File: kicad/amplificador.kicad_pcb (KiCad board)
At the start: 2 copper layers, 55 parts, among them Q1 BC557, Q10 BC547, Q11 BC547, Q12 BC557, Q13 BC547, Q14 BC557, Q15 TIP41C, Q16 TIP41C, Q17 TIP42C, Q18 TIP42C, Q2 BC547, Q3 BC557, Q4 BC547, Q5 BC557, Q6 BC557, Q7 BC547, Q8 BC557, Q9 BC547

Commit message: pcb Kicad actualizado
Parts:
- moved D4 360.7 mm to (203.2, 123.8)
- moved D3 327.1 mm to (205.7, 64.8)
- moved D6 264.2 mm to (266.7, 84.5)
- moved Q13 259.2 mm to (226.1, 81.3), turned to 270 degrees
- moved R15 255.5 mm to (112.4, 122.6), turned to 270 degrees
- moved Q17 228.8 mm to (246.4, 108.6), turned to 90 degrees
- moved Q10 214.9 mm to (179.1, 103.5), turned to 180 degrees
- moved Q16 203.0 mm to (245.7, 83.8), turned to 270 degrees
- moved R16 184.1 mm to (188.6, 113.7)
- moved R17 182.7 mm to (199.6, 117.5)
- moved Q12 175.9 mm to (226.7, 125.1), turned to 90 degrees
- moved Q18 171.9 mm to (244.5, 122.6), turned to 270 degrees
- moved R20 158.0 mm to (214.2, 111.8), turned to 180 degrees
- moved R8 157.2 mm to (214.2, 100.3), turned to 0 degrees
- moved R11 155.4 mm to (214.4, 104.8), turned to 0 degrees
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
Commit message: Primer ruteo
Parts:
- moved D5 91.3 mm to (184.2, 113.0)
- moved D6 90.4 mm to (176.8, 94.0)
- moved R21 85.4 mm to (176.3, 79.3)
- moved R22 81.4 mm to (176.5, 128.8)
- moved Q15 79.0 mm to (167.9, 77.1)
- moved Q16 78.2 mm to (167.9, 91.3)
- moved R23 78.2 mm to (168.5, 104.0)
- moved Q18 78.0 mm to (166.6, 127.5)
- moved Q17 77.3 mm to (169.7, 118.1)
- moved Q6 75.9 mm to (133.2, 79.5)
- moved D4 71.8 mm to (131.6, 129.4)
- moved Q12 71.6 mm to (155.2, 129.4), turned to 0 degrees
- moved Q11 71.1 mm to (156.8, 82.2)
- moved Q13 69.9 mm to (156.8, 91.3)
- moved Q14 69.9 mm to (157.5, 123.1)
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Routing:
- net V-: track 0.00 -> 149.8 mm
- net V+: track 0.00 -> 86.2 mm
- net Net-(C5-Pad2): track 0.00 -> 71.6 mm
- net Net-(Q5-Pad2): track 0.00 -> 62.1 mm, vias 0 -> 1
- net GND: track 0.00 -> 57.6 mm
- net Net-(C6-Pad2): track 0.00 -> 57.2 mm
- net Net-(C6-Pad1): track 0.00 -> 46.9 mm
- net Net-(D5-Pad2): track 0.00 -> 36.1 mm
- net Net-(Q14-Pad3): track 0.00 -> 33.9 mm
- net Net-(C2-Pad1): track 0.00 -> 33.3 mm
- net Net-(D6-Pad1): track 0.00 -> 31.1 mm
- net Net-(C5-Pad1): track 0.00 -> 29.9 mm
- net Net-(Q13-Pad3): track 0.00 -> 29.2 mm
- net Net-(Q7-Pad3): track 0.00 -> 25.2 mm
- net Net-(D3-Pad1): track 0.00 -> 23.8 mm
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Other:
- board outline added: 175.9 x 76.8 mm

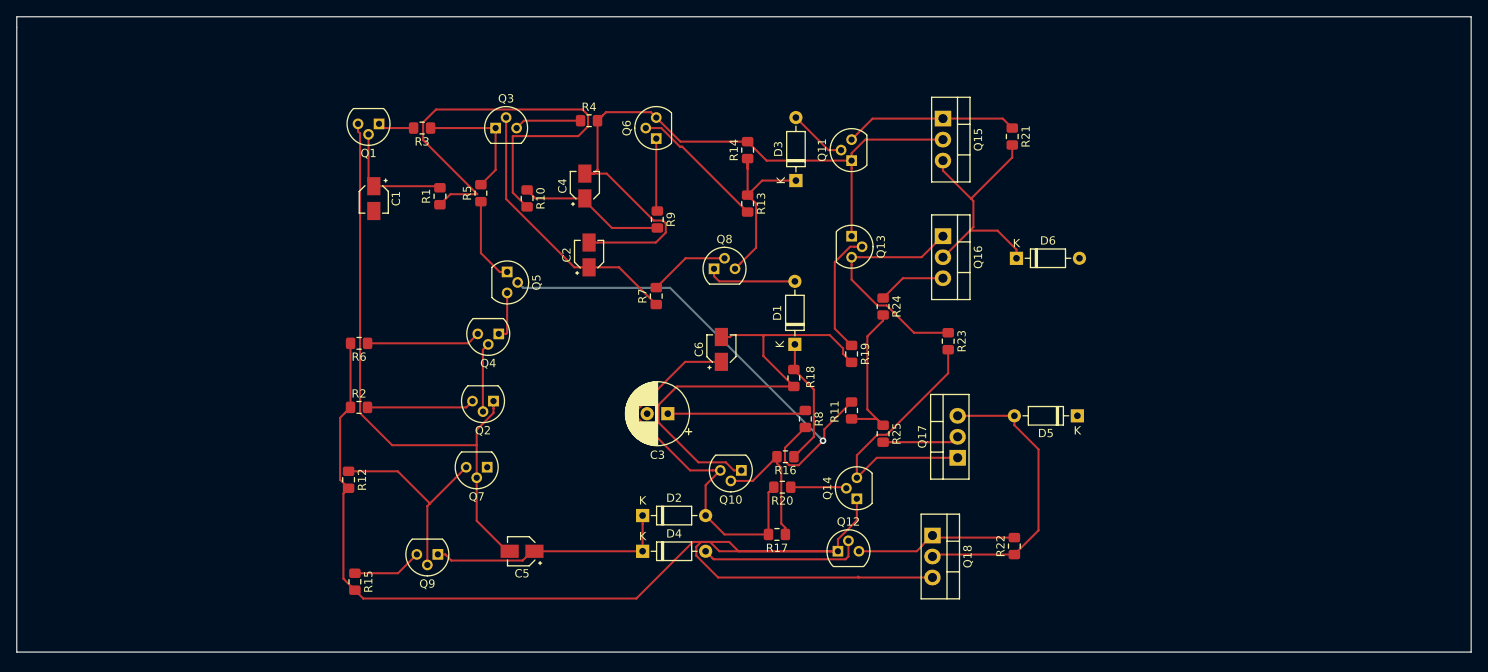
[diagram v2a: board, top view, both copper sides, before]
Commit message: Actualización del pcb
Se acercaró el multiplicador de vbe a los transistores de potencia por acoplamiento térmico. Se dejó lugar para montarlos sobre un disipador.
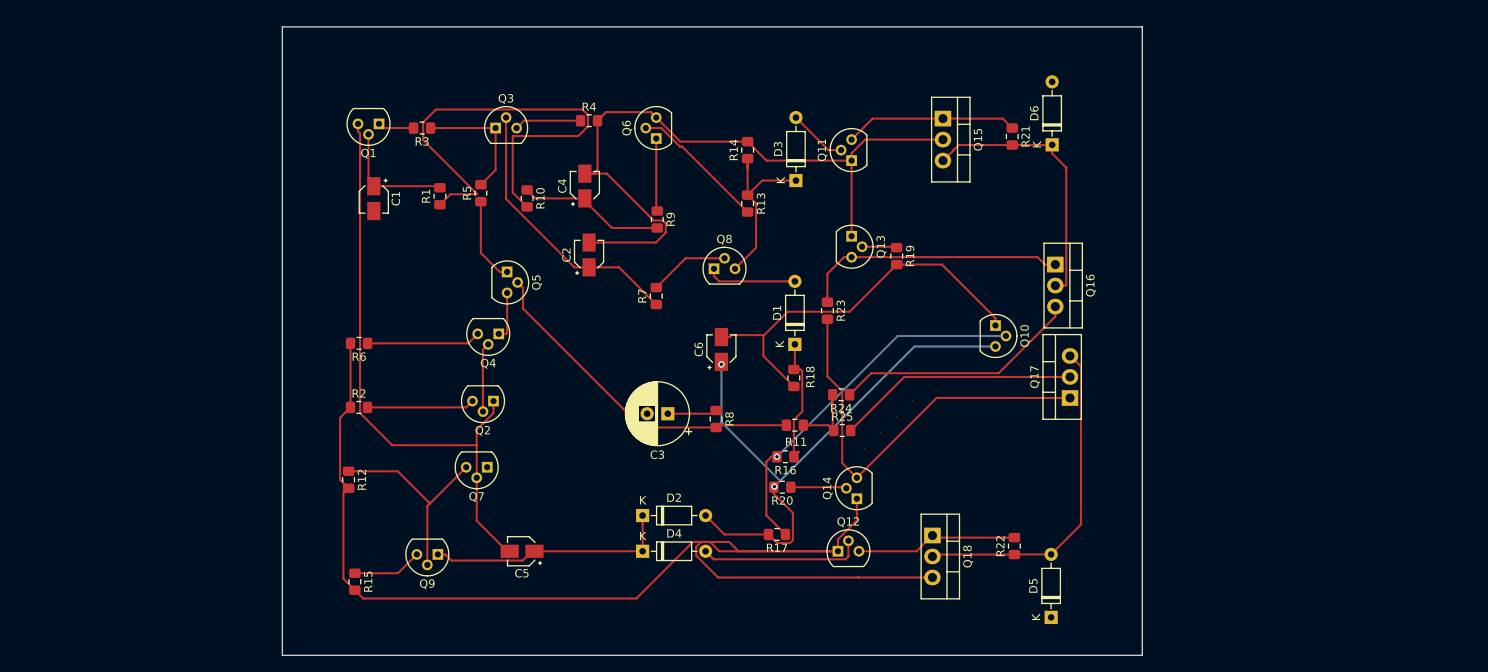
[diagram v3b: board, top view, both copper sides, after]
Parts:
- moved Q10 35.4 mm to (174.2, 102.1), turned to 270 degrees
- moved D5 24.6 mm to (181.0, 137.4), turned to 90 degrees
- moved Q17 15.4 mm to (183.3, 110.9)
- moved R23 15.1 mm to (153.9, 100.3)
- moved D6 14.4 mm to (181.1, 80.3), turned to 90 degrees
- moved Q16 14.0 mm to (181.5, 94.7)
- moved R19 13.0 mm to (162.3, 93.7)
- moved R24 11.8 mm to (155.6, 110.5), turned to 180 degrees
- moved R8 10.8 mm to (140.5, 113.4)
- moved R11 7.09 mm to (150.0, 114.2), turned to 180 degrees
- moved R25 4.96 mm to (155.7, 114.8), turned to 0 degrees
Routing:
- net Net-(Q10-Pad2): track 17.3 -> 45.7 mm, vias 0 -> 1
- net Net-(C6-Pad1): track 46.9 -> 71.1 mm, vias 0 -> 3
- net Net-(Q16-Pad3): track 8.23 -> 30.0 mm
- net Net-(Q5-Pad2): track 62.1 -> 41.7 mm, vias 1 -> 0
- net Net-(Q17-Pad2): track 9.29 -> 29.2 mm
- net Net-(Q14-Pad3): track 33.9 -> 50.4 mm
- net Net-(C3-Pad1): track 16.8 -> 6.00 mm
- net Net-(Q13-Pad2): track 15.0 -> 4.24 mm
- net Vout: track 19.0 -> 8.31 mm
- net Net-(C6-Pad2): track 57.2 -> 48.0 mm
- net Net-(D5-Pad2): track 36.1 -> 40.5 mm
- net Net-(Q13-Pad3): track 29.2 -> 32.2 mm
- net Net-(D6-Pad1): track 31.1 -> 33.0 mm
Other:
- board size 175.9 x 76.8 mm -> 104 x 76 mm

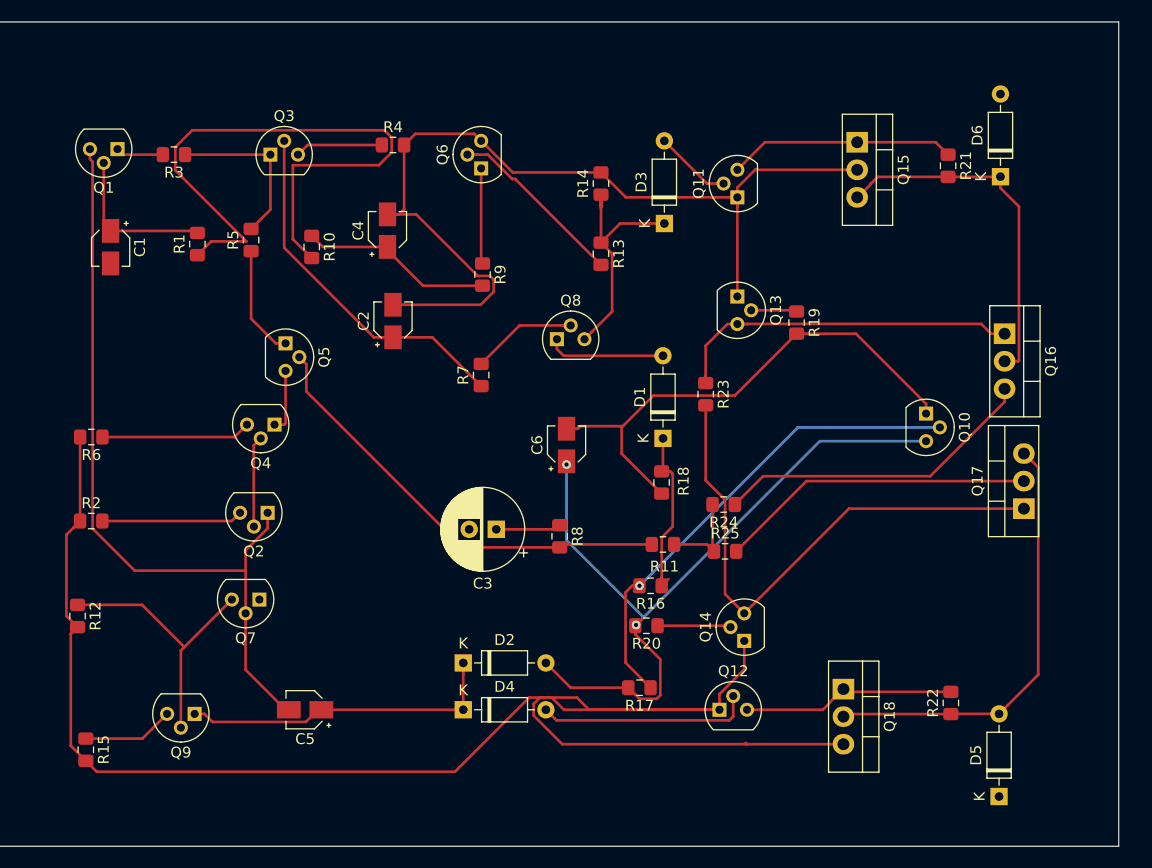
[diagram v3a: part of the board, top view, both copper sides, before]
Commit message: Ruteo del esquemático modificado
Capacitor a -30V, encapsulados finales, capacitor de entrada de poliéster.
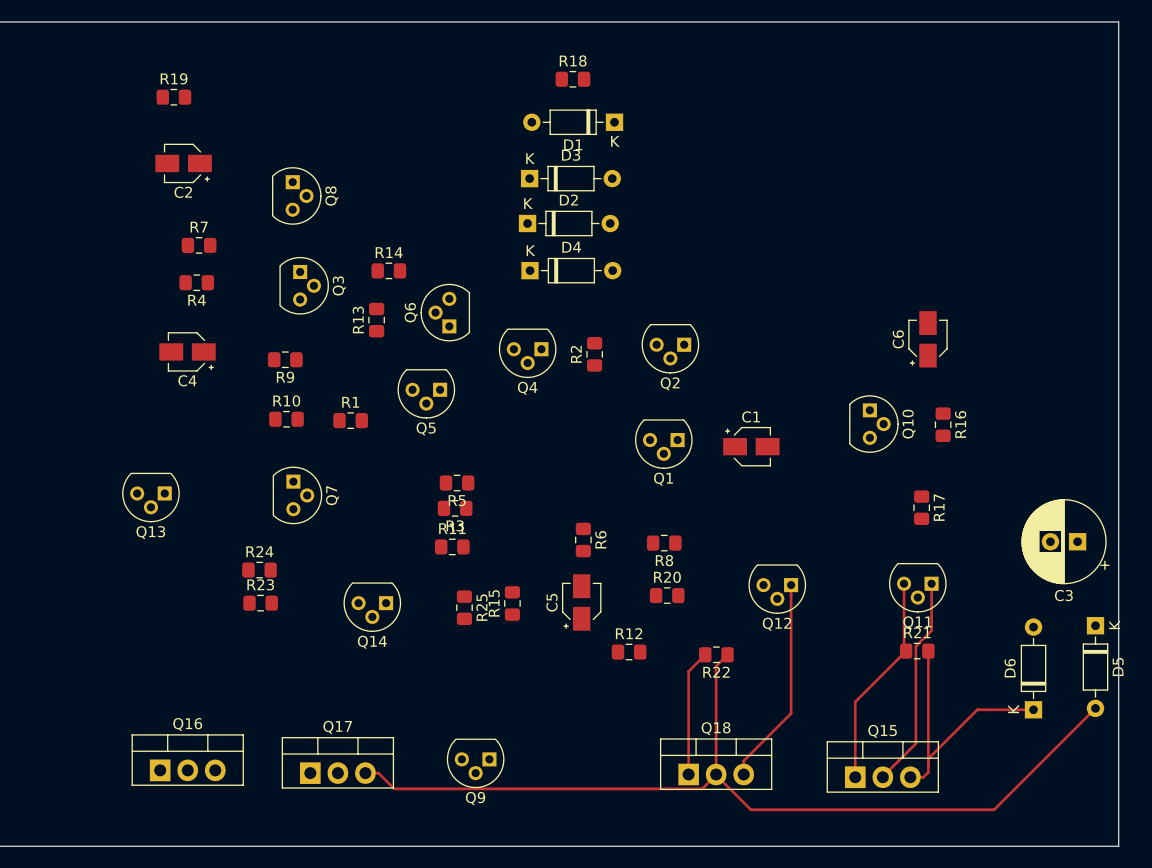
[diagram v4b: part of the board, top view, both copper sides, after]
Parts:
- moved Q16 87.6 mm to (103.6, 135.0), turned to 0 degrees
- moved Q17 70.2 mm to (117.5, 135.3), turned to 0 degrees
- moved C1 61.9 mm to (158.1, 105.2), turned to 0 degrees
- moved R19 61.1 mm to (104.9, 72.9), turned to 0 degrees
- moved Q15 58.5 mm to (167.7, 135.6), turned to 0 degrees
- moved Q1 58.2 mm to (151.3, 104.5)
- moved Q13 55.8 mm to (104.1, 109.5), turned to 180 degrees
- moved C3 53.6 mm to (188.2, 113.9)
- moved R12 51.0 mm to (146.9, 124.1), turned to 0 degrees
- moved D6 49.2 mm to (184.2, 129.4)
- moved R2 48.9 mm to (143.7, 96.6), turned to 90 degrees
- moved R6 46.3 mm to (142.6, 113.8), turned to 270 degrees
- moved R23 45.3 mm to (112.9, 119.6), turned to 0 degrees
- moved R21 44.8 mm to (173.4, 124.0), turned to 0 degrees
- moved R24 43.2 mm to (112.8, 116.5), turned to 0 degrees
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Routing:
- net V-: track 149.8 -> 19.3 mm
- net Net-(C5-Pad2): track 71.6 -> 0.00 mm
- net Net-(C6-Pad1): track 71.1 -> 0.00 mm, vias 3 -> 0
- net V+: track 86.2 -> 19.7 mm
- net GND: track 57.6 -> 0.00 mm
- net Net-(Q14-Pad3): track 50.4 -> 0.00 mm
- net Net-(C6-Pad2): track 48.0 -> 0.00 mm
- net Net-(Q10-Pad2): track 45.7 -> 0.00 mm, vias 1 -> 0
- net Net-(D5-Pad2): track 40.5 -> 85.2 mm
- net Net-(Q5-Pad2): track 41.7 -> 0.00 mm
- net Net-(C2-Pad1): track 33.3 -> 0.00 mm
- net Net-(Q13-Pad3): track 32.2 -> 0.00 mm
- net Net-(Q16-Pad3): track 30.0 -> 0.00 mm
- net Net-(C5-Pad1): track 29.9 -> 0.00 mm
- net Net-(Q17-Pad2): track 29.2 -> 0.00 mm
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
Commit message: viaje en el tiempo... el commit anterior esta roto
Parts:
- moved Q16 87.6 mm to (181.5, 94.7), turned to 270 degrees
- moved Q17 70.2 mm to (183.3, 110.9), turned to 90 degrees
- moved C1 61.9 mm to (99.1, 86.8), turned to 270 degrees
- moved R19 61.1 mm to (162.3, 93.7), turned to 270 degrees
- moved Q15 58.5 mm to (167.9, 77.1), turned to 270 degrees
- moved Q1 58.2 mm to (99.7, 77.7)
- moved Q13 55.8 mm to (156.8, 91.3), turned to 270 degrees
- moved C3 53.6 mm to (134.6, 112.8)
- moved R12 51.0 mm to (96.0, 120.8), turned to 270 degrees
- moved D6 49.2 mm to (181.1, 80.3)
- moved R2 48.9 mm to (97.3, 112.0), turned to 0 degrees
- moved R6 46.3 mm to (97.3, 104.3), turned to 180 degrees
- moved R23 45.3 mm to (153.9, 100.3), turned to 270 degrees
- moved R21 44.8 mm to (176.3, 79.3), turned to 270 degrees
- moved R24 43.2 mm to (155.6, 110.5), turned to 180 degrees
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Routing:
- net V-: track 19.3 -> 149.8 mm
- net Net-(C5-Pad2): track 0.00 -> 71.6 mm
- net Net-(C6-Pad1): track 0.00 -> 71.1 mm, vias 0 -> 3
- net V+: track 19.7 -> 86.2 mm
- net GND: track 0.00 -> 57.6 mm
- net Net-(Q14-Pad3): track 0.00 -> 50.4 mm
- net Net-(C6-Pad2): track 0.00 -> 48.0 mm
- net Net-(Q10-Pad2): track 0.00 -> 45.7 mm, vias 0 -> 1
- net Net-(D5-Pad2): track 85.2 -> 40.5 mm
- net Net-(Q5-Pad2): track 0.00 -> 41.7 mm
- net Net-(C2-Pad1): track 0.00 -> 33.3 mm
- net Net-(Q13-Pad3): track 0.00 -> 32.2 mm
- net Net-(Q16-Pad3): track 0.00 -> 30.0 mm
- net Net-(C5-Pad1): track 0.00 -> 29.9 mm
- net Net-(Q17-Pad2): track 0.00 -> 29.2 mm
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
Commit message: Final de clase viernes  28 de junio
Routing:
- net GND: track 57.6 -> 0.00 mm
- net Net-(C6-Pad1): track 71.1 -> 75.5 mm, vias 3 -> 2
- added copper zone on B.Cu, net GND

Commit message: carpeta kicad con esquematico con todos los encapsulados correctos, jumpers, pines de alimentacion y medicon. pcb a medio hacer
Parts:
- removed D1, D2: 1N4148, Diode_THT:D_DO-35_SOD27_P7.62mm_Horizontal
- added J1: Screw_Terminal_01x01, Connector_Wire:SolderWirePad_1x01_Drill0.8mm, F.Cu at (10.2, 101.6)
- added J10: Conn_01x01_Male, Connector_Pin:Pin_D0.7mm_L6.5mm_W1.8mm_FlatFork, F.Cu at (201.9, -12.7)
- added J11: Conn_01x01_Male, Connector_Pin:Pin_D0.7mm_L6.5mm_W1.8mm_FlatFork, F.Cu at (203.7, 116.3)
- added J12: Conn_01x01_Male, Connector_Pin:Pin_D0.7mm_L6.5mm_W1.8mm_FlatFork, F.Cu at (196.3, 128.0)
- added J13: Conn_01x01_Male, Connector_Pin:Pin_D0.7mm_L6.5mm_W1.8mm_FlatFork, F.Cu at (232.4, 71.1)
- added J14: Conn_01x01_Male, Connector_Pin:Pin_D0.7mm_L6.5mm_W1.8mm_FlatFork, F.Cu at (203.7, 122.9)
- added J15: Conn_01x01_Male, Connector_Pin:Pin_D0.7mm_L6.5mm_W1.8mm_FlatFork, F.Cu at (225.3, 104.6)
- added J16: Screw_Terminal_01x01, Connector_Wire:SolderWirePad_1x01_Drill0.8mm, F.Cu at (193.3, 135.4)
- added J17: Screw_Terminal_01x01, Connector_Wire:SolderWirePad_1x01_Drill0.8mm, F.Cu at (232.1, 98.0)
- added J2: Conn_01x01_Male, Connector_Pin:Pin_D0.7mm_L6.5mm_W1.8mm_FlatFork, F.Cu at (35.6, 83.8)
- added J3: Conn_01x01_Male, Connector_Pin:Pin_D0.7mm_L6.5mm_W1.8mm_FlatFork, F.Cu at (35.6, 134.6)
- added J4: Conn_01x01_Male, Connector_Pin:Pin_D0.7mm_L6.5mm_W1.8mm_FlatFork, F.Cu at (43.2, 33.0)
- added J5: Conn_01x01_Male, Connector_Pin:Pin_D0.7mm_L6.5mm_W1.8mm_FlatFork, F.Cu at (59.7, 83.8)
- added J6: Conn_01x01_Male, Connector_Pin:Pin_D0.7mm_L6.5mm_W1.8mm_FlatFork, F.Cu at (209.7, 109.8)
- added J7: Screw_Terminal_01x01, Connector_Wire:SolderWirePad_1x01_Drill0.8mm, F.Cu at (223.5, 1.27)
- added J8: Screw_Terminal_01x01, Connector_Wire:SolderWirePad_1x01_Drill0.8mm, F.Cu at (189.7, 128.9)
- added J9: Conn_01x01_Male, Connector_Pin:Pin_D0.7mm_L6.5mm_W1.8mm_FlatFork, F.Cu at (134.6, 34.3)
- added JP1: Jumper_NO_Small, kicad:SolderJumper-2_P1.3mm_Open_Pad1.0x1.5mm, F.Cu at (115.6, 99.1)
- added JP2: Jumper_NO_Small, kicad:SolderJumper-2_P1.3mm_Open_Pad1.0x1.5mm, F.Cu at (331.5, 86.4)
- added JP3: Jumper_NO_Small, kicad:SolderJumper-2_P1.3mm_Open_Pad1.0x1.5mm, F.Cu at (151.1, 106.7)
- added JP4: Jumper_NO_Small, kicad:SolderJumper-2_P1.3mm_Open_Pad1.0x1.5mm, F.Cu at (235.6, 142.2)
- added JP5: Jumper_NO_Small, kicad:SolderJumper-2_P1.3mm_Open_Pad1.0x1.5mm, F.Cu at (211.5, 14.0)
- added U1: LM385D-1.2, Package_SO:SOIC-8_3.9x4.9mm_P1.27mm, F.Cu at (273.0, 95.9)
- added U2: LM385D-1.2, Package_SO:SOIC-8_3.9x4.9mm_P1.27mm, F.Cu at (176.5, 3.81)
- C1: value 47u -> 10u; footprint Capacitor_SMD:CP_Elec_3x5.3 -> Capacitor_THT:C_Disc_D10.0mm_W2.5mm_P5.00mm
- D5, D6: value 1N4148 -> 1N5822; footprint Diode_THT:D_DO-35_SOD27_P7.62mm_Horizontal -> Diode_THT:D_DO-201AD_P15.24mm_Horizontal
- Q1, Q3, Q5, Q6, Q8: value BC557 -> MPSA92; footprint Package_TO_SOT_THT:TO-92 -> Package_TO_SOT_THT:TO-92_Inline
- Q10, Q2, Q4, Q7, Q9: value BC547 -> MPSA42; footprint Package_TO_SOT_THT:TO-92 -> Package_TO_SOT_THT:TO-92_Inline
- Q11, Q13: value BC547 -> BD135; footprint Package_TO_SOT_THT:TO-92 -> Package_TO_SOT_THT:TO-126-3_Vertical
- Q12, Q14: value BC557 -> BD136; footprint Package_TO_SOT_THT:TO-92 -> Package_TO_SOT_THT:TO-126-3_Vertical
- Q15, Q16: value TIP41C -> 2SD1047; footprint Package_TO_SOT_THT:TO-220-3_Vertical -> Package_TO_SOT_THT:TO-3PB-3_Vertical
- Q17, Q18: value TIP42C -> 2SB817; footprint Package_TO_SOT_THT:TO-220-3_Vertical -> Package_TO_SOT_THT:TO-3PB-3_Vertical
- R11: value 400 -> 12k
- R2, R6: value 1 -> 68
- R8: value 9.6k -> 470
- moved D4 218.7 mm to (185.4, -82.5)
- moved Q14 207.6 mm to (353.1, 53.3), turned to 0 degrees
- moved R25 203.6 mm to (359.2, 106.7)
- moved D3 201.8 mm to (351.8, 92.7), turned to 0 degrees
- moved R15 201.6 mm to (298.2, 142.2), turned to 0 degrees
- moved Q11 190.3 mm to (344.2, 115.6), turned to 0 degrees
- moved D5 190.2 mm to (336.6, 27.9), turned to 0 degrees
- moved C4 188.5 mm to (210.6, -82.5), turned to 0 degrees
- moved Q12 187.0 mm to (142.2, -57.1)
- moved R12 170.3 mm to (265.7, 135.9), turned to 0 degrees
- moved D6 166.9 mm to (348.0, 83.8), turned to 0 degrees
- moved Q17 165.9 mm to (332.4, 38.1), turned to 0 degrees
- moved R13 161.0 mm to (292.1, 151.1), turned to 0 degrees
- moved Q6 156.1 mm to (275.6, 143.5), turned to 0 degrees
- moved C6 153.3 mm to (146.1, -48.3), turned to 0 degrees
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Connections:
- C1 pad 2: Vin -> Net-(C1-Pad2)
- C2 pad 2: V+ -> Net-(C2-Pad2)
- C4 pad 2: V+ -> Net-(C2-Pad2)
- D5 pad 1: V1- -> Net-(D5-Pad1)
- D6 pad 2: V1+ -> Net-(D6-Pad2)
- Q10 pad 1: Net-(C6-Pad2) -> Net-(Q10-Pad1)
- Q10 pad 3: Net-(C6-Pad1) -> Net-(C5-Pad1)
- Q11 pad 1: V+ -> Net-(Q11-Pad1)
- Q11 pad 2: Net-(D3-Pad2) -> Net-(C2-Pad2)
- Q11 pad 3: Net-(Q11-Pad3) -> Net-(D3-Pad2)
- Q12 pad 1: V- -> Net-(Q12-Pad1)
- Q12 pad 2: Net-(D4-Pad2) -> Net-(J7-Pad1)
- Q12 pad 3: Net-(Q12-Pad3) -> Net-(D4-Pad2)
- Q13 pad 1: V+ -> Net-(J12-Pad1)
- Q13 pad 2: Net-(Q13-Pad2) -> Net-(C2-Pad2)
- Q13 pad 3: Net-(Q13-Pad3) -> Net-(J10-Pad1)
- Q14 pad 1: V- -> Net-(J13-Pad1)
- Q14 pad 2: Net-(Q14-Pad2) -> Net-(J7-Pad1)
- Q14 pad 3: Net-(Q14-Pad3) -> Net-(J11-Pad1)
- Q15 pad 1: Net-(Q11-Pad3) -> Net-(Q11-Pad1)
- Q15 pad 2: V+ -> Net-(C2-Pad2)
- Q16 pad 1: Net-(Q13-Pad3) -> Net-(J12-Pad1)
- Q17 pad 1: Net-(Q14-Pad3) -> Net-(J13-Pad1)
- Q17 pad 2: Net-(Q17-Pad2) -> Net-(D5-Pad2)
- Q17 pad 3: Net-(D5-Pad2) -> Net-(J15-Pad1)
- Q18 pad 1: Net-(Q12-Pad3) -> Net-(Q12-Pad1)
- Q18 pad 2: Net-(D5-Pad2) -> Net-(J7-Pad1)
- Q18 pad 3: V- -> Net-(D5-Pad2)
- Q2 pad 1: Net-(C5-Pad2) -> Net-(J3-Pad1)
- Q2 pad 3: Net-(Q2-Pad3) -> Net-(C5-Pad2)
- Q3 pad 1: Net-(Q3-Pad1) -> Net-(J4-Pad1)
- Q4 pad 1: Net-(Q2-Pad2) -> Net-(J6-Pad1)
- Q4 pad 3: Net-(Q4-Pad3) -> Net-(Q2-Pad2)
- Q6 pad 1: Net-(Q6-Pad1) -> Net-(C2-Pad2)
- Q6 pad 3: V+ -> Net-(Q6-Pad3)
- Q7 pad 1: GND -> Net-(Q10-Pad2)
- Q7 pad 3: Net-(Q7-Pad3) -> GND
- Q8 pad 1: Net-(D1-Pad2) -> Net-(D3-Pad1)
- Q8 pad 3: Net-(D3-Pad1) -> Net-(JP3-Pad1)
- Q9 pad 1: Net-(C5-Pad1) -> Net-(C6-Pad1)
- Q9 pad 2: Net-(Q7-Pad3) -> Net-(Q9-Pad2)
- Q9 pad 3: Net-(Q9-Pad3) -> Net-(C6-Pad2)
- R11 pad 1: Vout -> Net-(JP1-Pad1)
- R12 pad 1: Net-(Q7-Pad3) -> Net-(Q10-Pad2)
- R12 pad 2: V- -> Net-(J7-Pad1)
- R14 pad 2: V+ -> Net-(C2-Pad2)
- R15 pad 1: Net-(Q9-Pad3) -> Net-(Q10-Pad1)
- R15 pad 2: V- -> Net-(J7-Pad1)
- R16 pad 2: Net-(Q10-Pad2) -> Net-(Q9-Pad2)
- R17 pad 1: Net-(Q10-Pad2) -> Net-(Q9-Pad2)
- R19 pad 1: Net-(Q13-Pad2) -> Net-(J10-Pad1)
- R2 pad 1: V- -> Net-(J7-Pad1)
- R2 pad 2: Net-(Q2-Pad3) -> Net-(J3-Pad1)
- R20 pad 1: Net-(Q14-Pad2) -> Net-(J11-Pad1)
- R21 pad 1: Net-(Q11-Pad3) -> Net-(Q11-Pad1)
- R22 pad 2: Net-(Q12-Pad3) -> Net-(Q12-Pad1)
- R23 pad 1: Net-(Q13-Pad3) -> Net-(J12-Pad1)
- R23 pad 2: Net-(Q14-Pad3) -> Net-(J13-Pad1)
- R24 pad 2: Vout -> Net-(JP2-Pad2)
- R25 pad 1: Vout -> Net-(JP2-Pad2)
- R25 pad 2: Net-(Q17-Pad2) -> Net-(J15-Pad1)
- R3 pad 1: Net-(Q3-Pad1) -> Net-(Q3-Pad3)
- R4 pad 1: Net-(Q3-Pad3) -> Net-(J4-Pad1)
- R4 pad 2: V+ -> Net-(C2-Pad2)
- R5 pad 2: Net-(Q3-Pad1) -> Net-(Q3-Pad3)
- R6 pad 1: Net-(Q4-Pad3) -> Net-(J6-Pad1)
- R6 pad 2: V- -> Net-(J7-Pad1)
- R9 pad 1: Net-(Q6-Pad1) -> Net-(Q6-Pad3)
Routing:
- net V-: track 149.8 -> 0.00 mm
- net V+: track 86.2 -> 0.00 mm
- net Net-(C6-Pad1): track 75.5 -> 0.00 mm, vias 2 -> 0
- net Net-(C5-Pad2): track 71.6 -> 0.00 mm
- net Net-(Q14-Pad3): track 50.4 -> 0.00 mm
- net Net-(C6-Pad2): track 48.0 -> 0.00 mm
- net Net-(Q10-Pad2): track 45.7 -> 0.00 mm, vias 1 -> 0
- net Net-(Q5-Pad2): track 41.7 -> 0.00 mm
- net Net-(D5-Pad2): track 40.5 -> 0.00 mm
- net Net-(C2-Pad1): track 33.3 -> 0.00 mm
- net Net-(D6-Pad1): track 33.0 -> 0.00 mm
- net Net-(Q13-Pad3): track 32.2 -> 0.00 mm
- net Net-(J14-Pad1): track 30.0 -> 0.00 mm
- net Net-(C5-Pad1): track 29.9 -> 0.00 mm
- net Net-(Q17-Pad2): track 29.2 -> 0.00 mm
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- removed copper zone on B.Cu, net GND
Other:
- board outline removed

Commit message: cambios en los jumpers, ruteo avanzado
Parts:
- removed JP5: Jumper_NO_Small, kicad:SolderJumper-2_P1.3mm_Open_Pad1.0x1.5mm
- added J18: Conn_01x01_Male, Connector_Pin:Pin_D0.7mm_L6.5mm_W1.8mm_FlatFork, F.Cu at (74.9, 83.8)
- moved J7 225.5 mm to (68.6, 165.1)
- moved R13 216.0 mm to (118.4, 22.9)
- moved Q6 213.5 mm to (100.3, 21.6), turned to 270 degrees
- moved D4 201.6 mm to (166.4, 118.1)
- moved R14 184.5 mm to (133.6, 11.4)
- moved C4 183.1 mm to (83.8, 49.5)
- moved D3 183.0 mm to (175.3, 44.5)
- moved Q12 181.1 mm to (188.0, 118.1), turned to 270 degrees
- moved R9 172.6 mm to (99.1, 49.8), turned to 270 degrees
- moved R12 169.2 mm to (96.5, 139.9), turned to 270 degrees
- moved R15 166.6 mm to (132.1, 129.5), turned to 270 degrees
- moved Q11 153.6 mm to (210.8, 39.4)
- moved J6 151.6 mm to (59.7, 132.1)
- moved JP4 147.7 mm to (120.7, 49.5)
- moved R16 146.9 mm to (119.4, 63.7), turned to 270 degrees
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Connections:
- JP3 pad 2: Net-(C5-Pad1) -> Net-(C5-Pad2)
- JP4 pad 1: Net-(JP4-Pad1) -> Net-(C4-Pad1)
- JP4 pad 2: Net-(C5-Pad1) -> Net-(JP4-Pad2)
- Q1 pad 3: Net-(C5-Pad2) -> Net-(JP3-Pad1)
- Q2 pad 3: Net-(C5-Pad2) -> Net-(JP3-Pad1)
- Q8 pad 3: Net-(JP3-Pad1) -> Net-(JP4-Pad2)
- U1 pad 8: Net-(JP5-Pad2) -> Net-(JP4-Pad2)
- U2 pad 4: Net-(JP4-Pad1) -> Net-(C5-Pad1)
